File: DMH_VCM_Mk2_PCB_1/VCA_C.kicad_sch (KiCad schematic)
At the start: 19 parts, among them Q5 BC548, Q6 BC548, U2 TL074

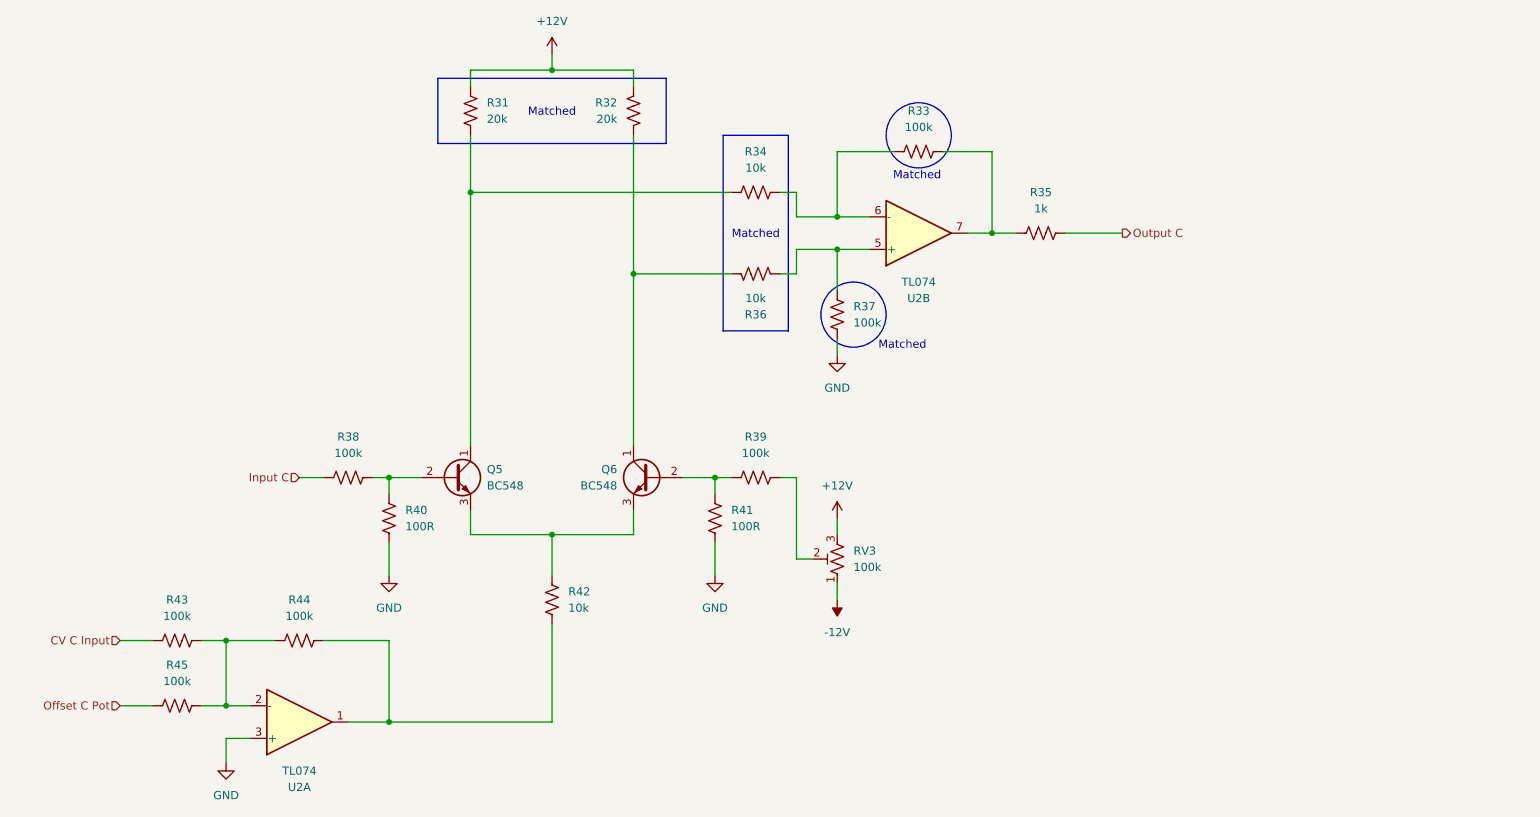
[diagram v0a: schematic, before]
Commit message: Almost finished PCB 1 schematic
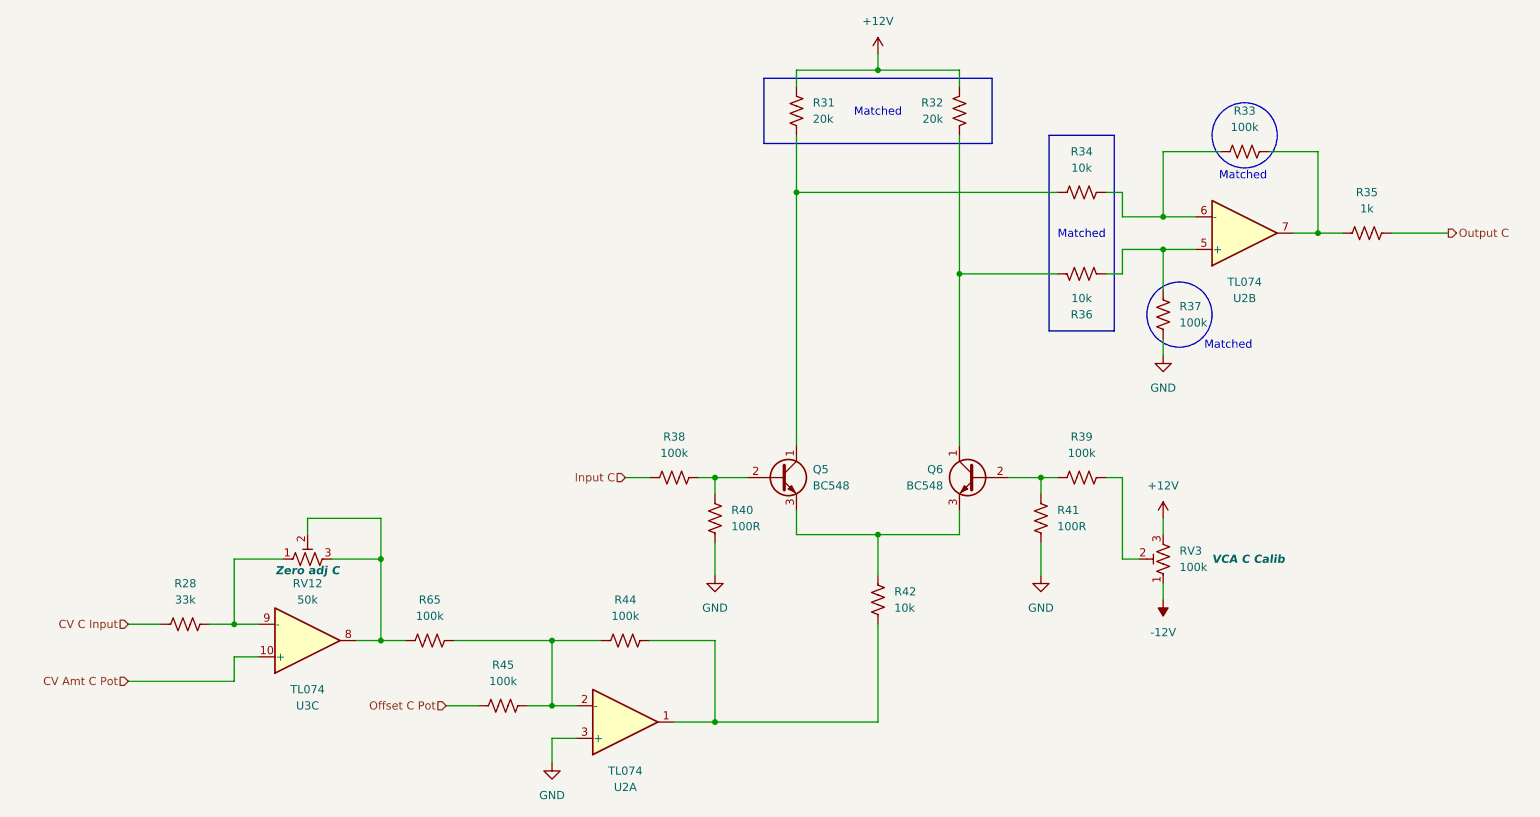
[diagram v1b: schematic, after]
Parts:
- removed R43: 100k, Resistor_THT:R_Axial_DIN0207_L6.3mm_D2.5mm_P2.54mm_Vertical, symbol Device:R_US
- added R28: 33k, Resistor_THT:R_Axial_DIN0207_L6.3mm_D2.5mm_P7.62mm_Horizontal, symbol Device:R_US
- added R65: 100k, Resistor_THT:R_Axial_DIN0207_L6.3mm_D2.5mm_P7.62mm_Horizontal, symbol Device:R_US
- added RV12: 50k, Potentiometer_THT:Potentiometer_Bourns_3296W_Vertical, symbol Device:R_Potentiometer_Trim_US
- added U3: TL074, Package_DIP:DIP-14_W7.62mm_Socket, symbol Amplifier_Operational:TL074
- RV3: Function (none) -> VCA C Calib
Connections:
- net CV C Input: now also R28.1
- net at R44.1, R45.2, U2.2 (-): now also R65.2
- new net: R65.1, RV12.2, RV12.3, U3.8
- new net: R28.2, RV12.1, U3.9 (-)
- new net CV Amt C Pot: U3.10 (+)
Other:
- moved on the sheet: Q5, Q6, R31, R32, R33, R34, R35, R36, R37, R38, R39, R40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

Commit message: PCB 1 placement in progress
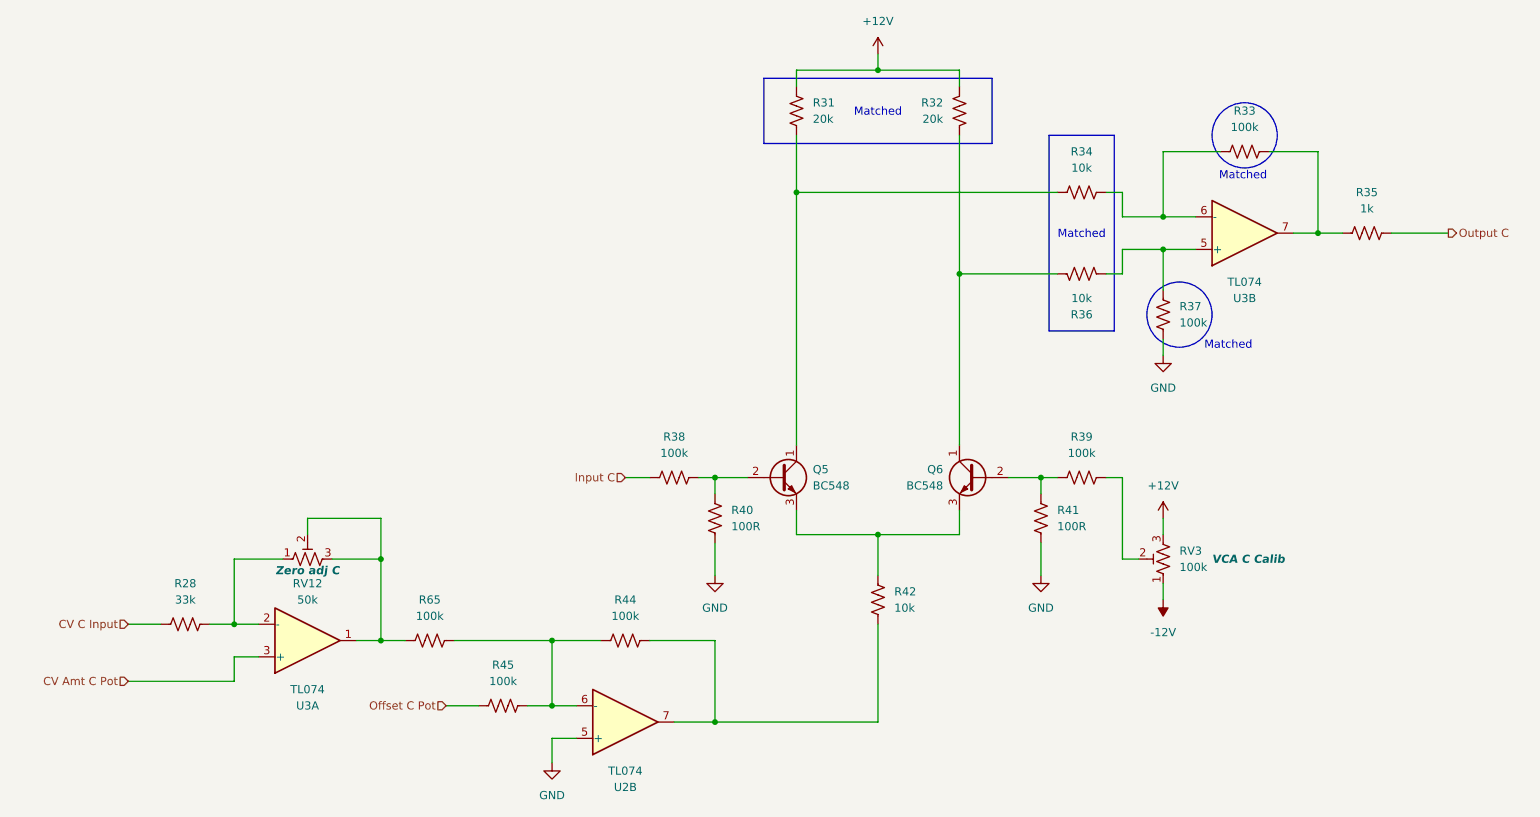
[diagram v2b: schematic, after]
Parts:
- R28, R65: footprint Resistor_THT:R_Axial_DIN0207_L6.3mm_D2.5mm_P7.62mm_Horizontal -> Resistor_THT:R_Axial_DIN0207_L6.3mm_D2.5mm_P2.54mm_Vertical
- renumbered U2 to U3
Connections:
- net CV Amt C Pot: now also U3.3 (+); no longer U3.10 (+)
- net GND: now also U2.5 (+); no longer U2.3 (+)
- net at R65.1, RV12.2, RV12.3: now also U3.1; no longer U3.8
- net at R28.2, RV12.1: now also U3.2 (-); no longer U3.9 (-)
- net at R44.1, R45.2, R65.2: now also U2.6 (-); no longer U2.2 (-)
- net at R42.1, R44.2: now also U2.7; no longer U2.1
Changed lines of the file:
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@@
 		(at 88.9 139.7 0)
 		(mirror x)
-		(unit 3)
+		(unit 1)
 		(exclude_from_sim no)
 		(in_bom yes)
@@
 				(path "/58f4306d-5387-4983-bb08-41a2313fd315/e5196600-83a1-4dc3-ad8c-62681c1f8ce4"
 					(reference "U3")
-					(unit 3)
+					(unit 1)
 				)
 			)
@@
 		(on_board yes)
 		(dnp no)
-		(property "Reference" "U2"
+		(property "Reference" "U3"
 			(at 234.95 86.36 0)
 			(effects
@@
 			(project "DMH_Tripple_VCA_PCB_1"
 				(path "/58f4306d-5387-4983-bb08-41a2313fd315/e5196600-83a1-4dc3-ad8c-62681c1f8ce4"
-					(reference "U2")
+					(reference "U3")
 					(unit 2)
 				)
@@
 			)
 		)
-		(property "Footprint" "Resistor_THT:R_Axial_DIN0207_L6.3mm_D2.5mm_P7.62mm_Horizontal"
+		(property "Footprint" "Resistor_THT:R_Axial_DIN0207_L6.3mm_D2.5mm_P2.54mm_Vertical"
 			(at 108.204 138.684 90)
 			(effects
@@
 		(at 138.43 152.4 0)
 		(mirror x)
-		(unit 1)
+		(unit 2)
 		(exclude_from_sim no)
 		(in_bom yes)
@@
 				(path "/58f4306d-5387-4983-bb08-41a2313fd315/e5196600-83a1-4dc3-ad8c-62681c1f8ce4"
 					(reference "U2")
-					(unit 1)
+					(unit 2)
 				)
 			)
@@
 			)
 		)
-		(property "Footprint" "Resistor_THT:R_Axial_DIN0207_L6.3mm_D2.5mm_P7.62mm_Horizontal"
+		(property "Footprint" "Resistor_THT:R_Axial_DIN0207_L6.3mm_D2.5mm_P2.54mm_Vertical"
 			(at 70.104 136.144 90)
 			(effects

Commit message: PCB 1 placement done
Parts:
- RV3: Function VCA C Calib -> Calib C
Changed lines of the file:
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@@
 			)
 		)
-		(property "Function" "VCA C Calib"
+		(property "Function" "Calib C"
 			(at 229.87 127 0)
 			(effects
